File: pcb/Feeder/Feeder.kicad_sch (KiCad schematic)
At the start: 5 parts, among them J1 Controller, J2 Servo, J3 Feedback, J4 N20

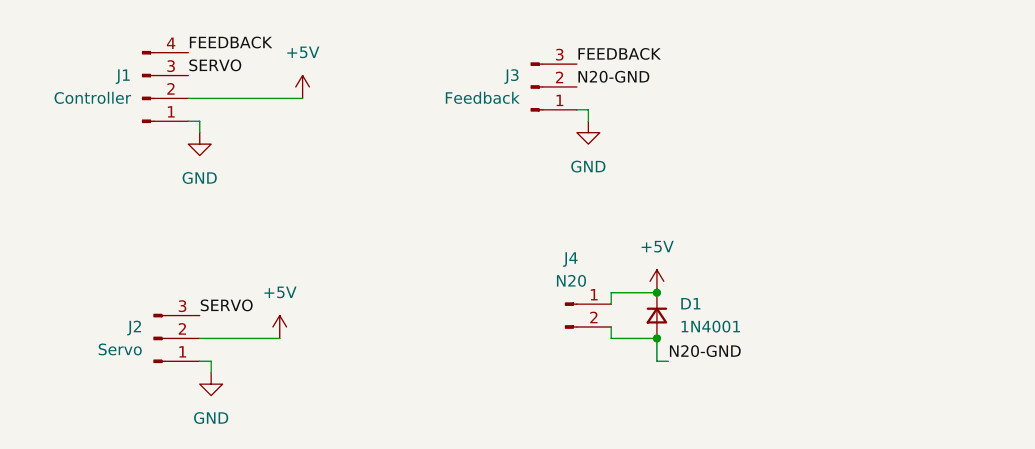
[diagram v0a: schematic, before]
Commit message: Update Feeder PCB to adjust footprints for clearances.
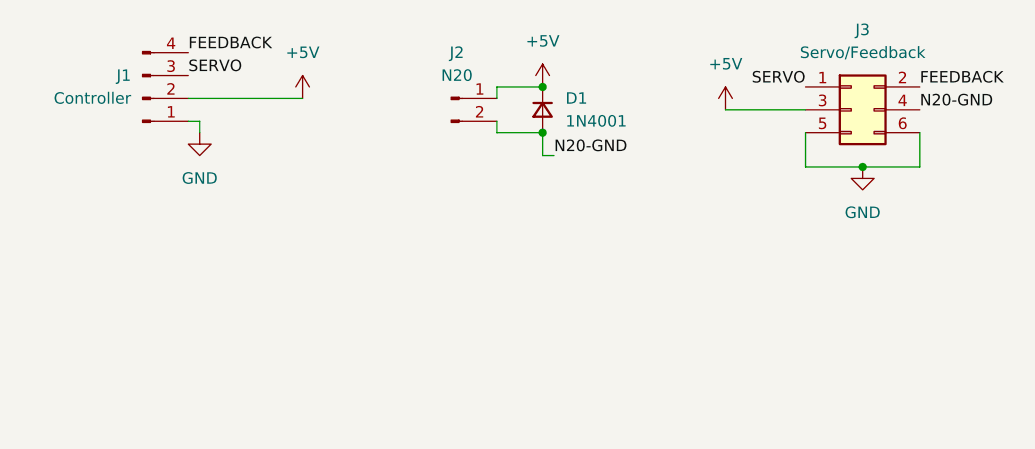
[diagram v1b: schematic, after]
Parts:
- removed J2: Servo, Connector_PinHeader_2.54mm:PinHeader_1x03_P2.54mm_Vertical, symbol Connector:Conn_01x03_Male
- removed J3: Feedback, Connector_PinHeader_2.54mm:PinHeader_1x03_P2.54mm_Vertical, symbol Connector:Conn_01x03_Male
- added J3: Servo/Feedback, Connector_PinHeader_2.54mm:PinHeader_2x03_P2.54mm_Vertical, symbol Connector_Generic:Conn_02x03_Odd_Even
- renumbered J4 to J2
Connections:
- net +5V: now also J3.3 (Pin_3)
- net FEEDBACK: now also J3.2 (Pin_2)
- net GND: now also J3.5 (Pin_5), J3.6 (Pin_6)
- net N20-GND: now also J3.4 (Pin_4)
- net SERVO: now also J3.1 (Pin_1)
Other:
- moved on the sheet: D1, J2

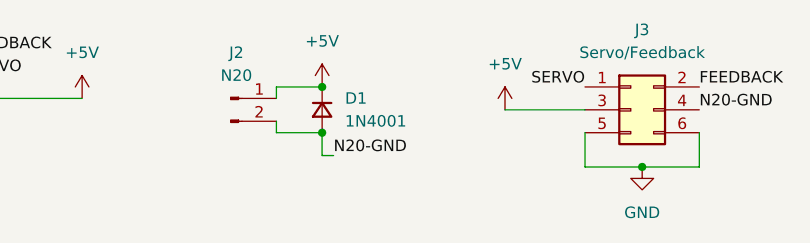
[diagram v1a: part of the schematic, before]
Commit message: Feeder - added optional THT diode footprint, repanelized
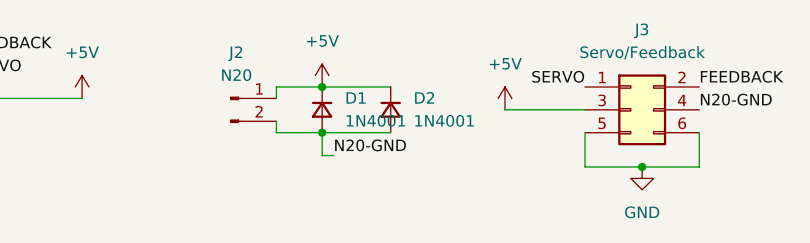
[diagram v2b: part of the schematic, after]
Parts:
- added D2: 1N4001, CustomDiode:D_SMA-SMB_Universal_Handsoldering_Holes, symbol Device:D_Small
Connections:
- net +5V: now also D2.1 (K)
- net N20-GND: now also D2.2 (A)
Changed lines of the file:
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@@
+    (stroke (width 0) (type default) (color 0 0 0 0))
+  )
+  (wire (pts (xy 110.49 57.15) (xy 118.11 57.15))
     (stroke (width 0) (type default) (color 0 0 0 0))
   )
@@
   )
   (wire (pts (xy 71.12 53.34) (xy 83.82 53.34))
+    (stroke (width 0) (type default) (color 0 0 0 0))
+  )
+  (wire (pts (xy 110.49 52.07) (xy 118.11 52.07))
     (stroke (width 0) (type default) (color 0 0 0 0))
   )
@@
     (pin "2")
   )
+  (symbol (lib_id "Device:D_Small") (at 118.11 54.61 270) (unit 1)
+    (in_bom yes) (on_board yes) (fields_autoplaced)
+    (property "Reference" "D2" (id 0) (at 120.65 53.3399 90)
+      (effects (font (size 1.27 1.27)) (justify left))
+    )
+    (property "Value" "1N4001" (id 1) (at 120.65 55.8799 90)
+      (effects (font (size 1.27 1.27)) (justify left))
+    )
+    (property "Footprint" "CustomDiode:D_SMA-SMB_Universal_Handsoldering_Holes" (id 2) (at 118.11 54.61 90)
+      (effects (font (size 1.27 1.27)) hide)
+    )
+    (property "Datasheet" "~" (id 3) (at 118.11 54.61 90)
+      (effects (font (size 1.27 1.27)) hide)
+    )
+    (pin "1")
+    (pin "2")
+  )
   (symbol (lib_id "power:GND") (at 146.05 60.96 0) (unit 1)
     (in_bom yes) (on_board yes) (fields_autoplaced)
@@
       (reference "D1") (unit 1) (value "1N4001") (footprint "Diode_SMD:D_SMA-SMB_Universal_Handsoldering")
     )
+    (path "/afed1c1b-60db-46a2-bdd9-90fa02d3f2be"
+      (reference "D2") (unit 1) (value "1N4001") (footprint "CustomDiode:D_SMA-SMB_Universal_Handsoldering_Holes")
+    )
     (path "/e5e10b7e-d4e1-472a-acd2-b7ba1a3292f0"

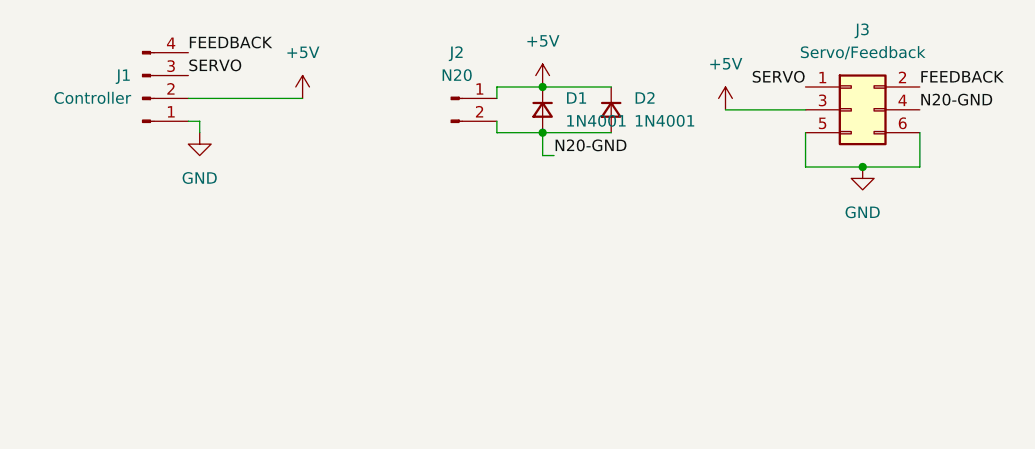
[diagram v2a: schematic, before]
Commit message: recreated feeder PCB for new 0816 CAD design (#5)
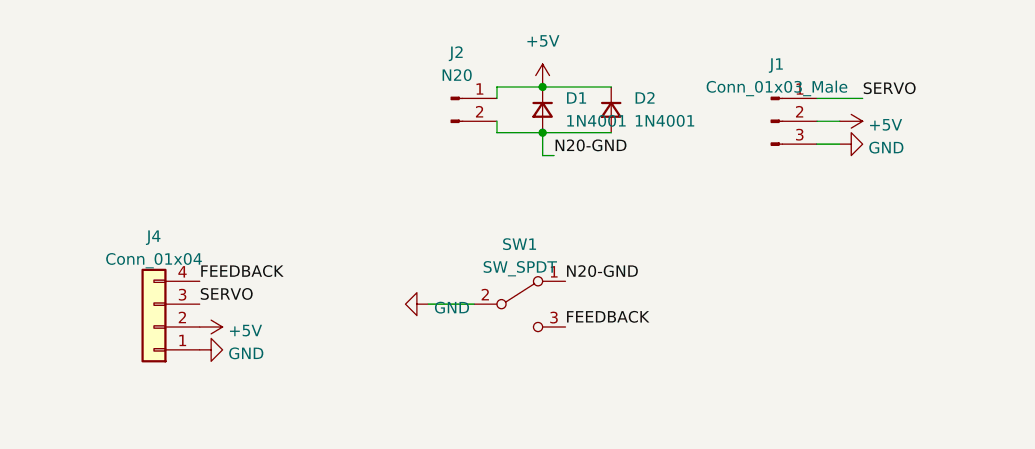
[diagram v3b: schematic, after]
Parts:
- removed J1: Controller, Connector_PinHeader_2.54mm:PinHeader_1x04_P2.54mm_Vertical, symbol Connector:Conn_01x04_Male
- removed J3: Servo/Feedback, Connector_PinHeader_2.54mm:PinHeader_2x03_P2.54mm_Vertical, symbol Connector_Generic:Conn_02x03_Odd_Even
- added J1: Conn_01x03_Male, PinsClean:PinSocket_1x03_P2.54mm_Vertical_Clean, symbol Connector:Conn_01x03_Male
- added J4: Conn_01x04, PinsClean:PinSocket_1x04_P2.54mm_Vertical_Clean, symbol Connector_Generic:Conn_01x04
- added SW1: SW_SPDT, Microswitch:Microswitch, symbol Switch:SW_SPDT
- D2: footprint CustomDiode:D_SMA-SMB_Universal_Handsoldering_Holes -> Diode_THT:D_A-405_P7.62mm_Horizontal
- J2: footprint Connector_JST:JST_PH_B2B-PH-K_1x02_P2.00mm_Vertical -> PinsClean:PinSocket_1x02_P2.54mm_Vertical_Clean
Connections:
- net +5V: now also J1.2 (Pin_2), J4.2 (Pin_2)
- net FEEDBACK: now also J4.4 (Pin_4), SW1.3 (C)
- net GND: now also J1.3 (Pin_3), J4.1 (Pin_1), SW1.2 (B)
- net N20-GND: now also SW1.1 (A)
- net SERVO: now also J1.1 (Pin_1), J4.3 (Pin_3)
